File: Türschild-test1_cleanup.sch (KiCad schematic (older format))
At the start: 96 parts, among them J1 662103130822smt, J2 Conn_01x03_Female, J3 USB_B_Micro, J4 Conn_01x24_MountingPin, J5 PROG, J6 Conn_01x08_Female, Q1 IRLML2502PbF, U1 BQ25570, U2 BQ27441-G1, U3 ESP32-WROOM-32, U4 CP2102N-A01-GQFN28, U5 LM1117-3.3, U6 WE-TVS-82400102

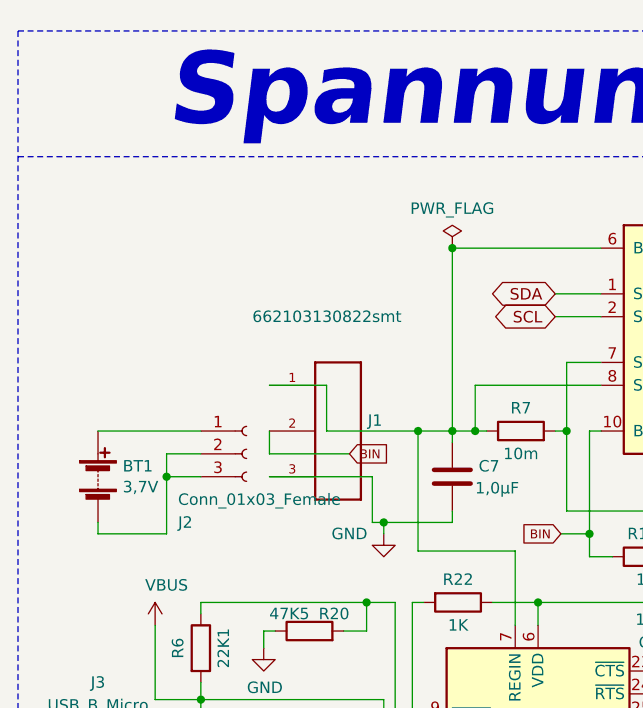
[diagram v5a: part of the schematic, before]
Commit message: Pull-Ups und Pull-Downs für die beiden USB-Datenleitungen eingebaut. nur 1K5 Wiederstand auf D+ gegen 3V3 wurde bestückt
neue Schaltplan und Layout für korrektour erstellt
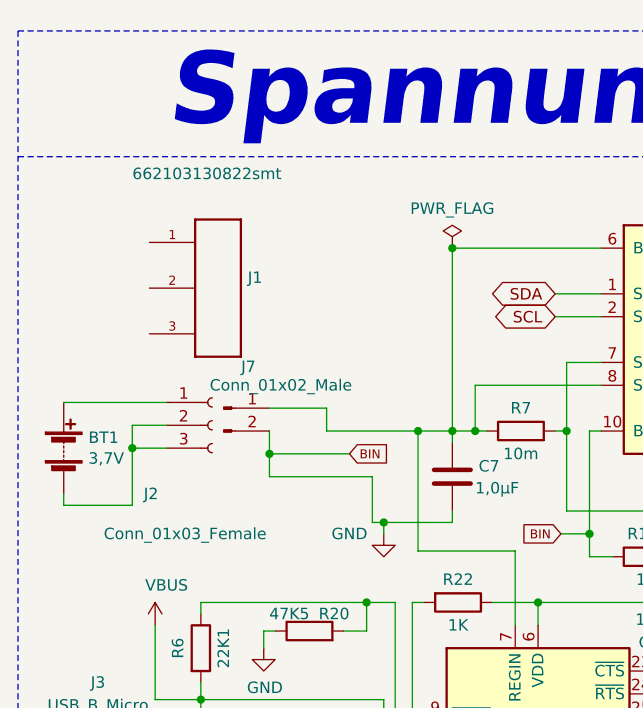
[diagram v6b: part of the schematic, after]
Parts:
- added J7: Conn_01x02_Male, Connector_Molex:Molex_PicoBlade_53047-0210_1x02_P1.25mm_Vertical, symbol Connector:Conn_01x02_Male
- J1: footprint Tuerschild-Kiacad:662103130822 -> Connector_Molex:Molex_PicoBlade_53047-0310_1x03_P1.25mm_Vertical
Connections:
- net GND: now also R19.1, U2.10 (BIN), J7.2 (Pin_2); no longer J1.3
- net at C7.1, R7.1, U2.6 (BAT)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: now also J7.1 (Pin_1); no longer J1.1
- removed net BIN: J1.2, R19.1, U2.10 (BIN)
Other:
- moved on the sheet: BT1, J1, J2
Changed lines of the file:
@@
 L Connector:Conn_01x03_Female J2
 U 1 1 5E741D88
-P 1650 2450
-F 0 "J2" H 1350 2150 50  0000 L CNN
-F 1 "Conn_01x03_Female" H 1350 2250 50  0000 L CNN
-F 2 "Connector_PinSocket_2.00mm:PinSocket_1x03_P2.00mm_Vertical_SMD_Pin1Right" H 1650 2450 50  0001 C CNN
-F 3 "~" H 1650 2450 50  0001 C CNN
-	1    1650 2450
-	1    0    0    -1
-$EndComp
-Wire Wire Line
-	1450 2350 1000 2350
-Wire Wire Line
-	1000 2750 1000 2800
-Wire Wire Line
-	1000 2800 1300 2800
-Wire Wire Line
-	1300 2800 1300 2550
-Wire Wire Line
-	1300 2550 1450 2550
-Wire Wire Line
-	1450 2450 1300 2450
-Wire Wire Line
-	1300 2450 1300 2550
-Connection ~ 1300 2550
+P 1500 2325
+F 0 "J2" H 1200 2025 50  0000 L CNN
+F 1 "Conn_01x03_Female" H 1025 1850 50  0000 L CNN
+F 2 "Connector_PinSocket_2.00mm:PinSocket_1x03_P2.00mm_Vertical_SMD_Pin1Right" H 1500 2325 50  0001 C CNN
+F 3 "~" H 1500 2325 50  0001 C CNN
+	1    1500 2325
+	1    0    0    -1
+$EndComp
+Wire Wire Line
+	1300 2225 850  2225
+Wire Wire Line
+	850  2625 850  2675
+Wire Wire Line
+	850  2675 1150 2675
+Wire Wire Line
+	1150 2675 1150 2425
+Wire Wire Line
+	1150 2425 1300 2425
+Wire Wire Line
+	1300 2325 1150 2325
+Wire Wire Line
+	1150 2325 1150 2425
+Connection ~ 1150 2425
 Wire Wire Line
 	3800 9750 4600 9750
@@
 L Device:Battery BT1
 U 1 1 5E2300F3
-P 1000 2550
-F 0 "BT1" H 1108 2596 50  0000 L CNN
-F 1 "3,7V" H 1108 2505 50  0000 L CNN
-F 2 "Battery:BatteryHolder_Bulgin_BX0036_1xC" V 1000 2610 50  0001 C CNN
-F 3 "~" V 1000 2610 50  0001 C CNN
-	1    1000 2550
+P 850 2425
+F 0 "BT1" H 958 2471 50  0000 L CNN
+F 1 "3,7V" H 958 2380 50  0000 L CNN
+F 2 "Battery:BatteryHolder_Bulgin_BX0036_1xC" V 850 2485 50  0001 C CNN
+F 3 "~" V 850 2485 50  0001 C CNN
+	1    850  2425
 	1    0    0    -1
 $EndComp
@@
 L Türschild-test1_cleanup-rescue:662103130822smt J1
 U 1 1 5FA25719
-P 2050 2350
-F 0 "J1" V 2004 2480 50  0000 L CNN
-F 1 "662103130822smt" V 1550 1975 50  0000 L CNN
-F 2 "Tuerschild-Kiacad:662103130822" H 2050 2350 50  0001 L BNN
-F 3 "" H 2050 2350 50  0001 C CNN
-	1    2050 2350
+P 1525 1725
+F 0 "J1" V 1479 1855 50  0000 L CNN
+F 1 "662103130822smt" V 1025 1350 50  0000 L CNN
+F 2 "Connector_Molex:Molex_PicoBlade_53047-0310_1x03_P1.25mm_Vertical" H 1525 1725 50  0001 L BNN
+F 3 "" H 1525 1725 50  0001 C CNN
+	1    1525 1725
 	0    1    1    0
 $EndComp
 Wire Wire Line
-	2000 2350 2000 2150
-Wire Wire Line
-	2000 2150 1750 2150
+	2000 2350 2000 2250
+Wire Wire Line
+	2000 2250 1750 2250
 Wire Wire Line
 	1750 2450 1750 2350
@@
 	8050 4350 7975 4350
 Connection ~ 7975 4350
+$Comp
+L Connector:Conn_01x02_Male J7
+U 1 1 5FCB9EE4
+P 1550 2250
+F 0 "J7" H 1658 2431 50  0000 C CNN
+F 1 "Conn_01x02_Male" H 1800 2350 50  0000 C CNN
+F 2 "Connector_Molex:Molex_PicoBlade_53047-0210_1x02_P1.25mm_Vertical" H 1550 2250 50  0001 C CNN
+F 3 "~" H 1550 2250 50  0001 C CNN
+	1    1550 2250
+	1    0    0    -1
+$EndComp
+Wire Wire Line
+	1750 2550 1750 2450
+Connection ~ 1750 2450
 $EndSCHEMATC
